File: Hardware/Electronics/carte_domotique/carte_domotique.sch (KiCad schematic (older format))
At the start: 21 parts, among them J1 Conn_02x06_Odd_Even, J10 Conn_01x04, J11 Conn_01x04, J12 Conn_01x04, J13 Conn_01x02, J14 Conn_01x02, J15 Conn_01x02, J16 Conn_01x02, J17 Conn_01x02, J18 Conn_01x02, J19 Conn_01x02, J2 Raspberry_Pi_2_3, J3 Conn_01x02, J4 Conn_01x05, J5 Conn_01x05, J6 Conn_01x03, J7 Conn_01x03, J8 Conn_01x03, J9 Conn_01x03

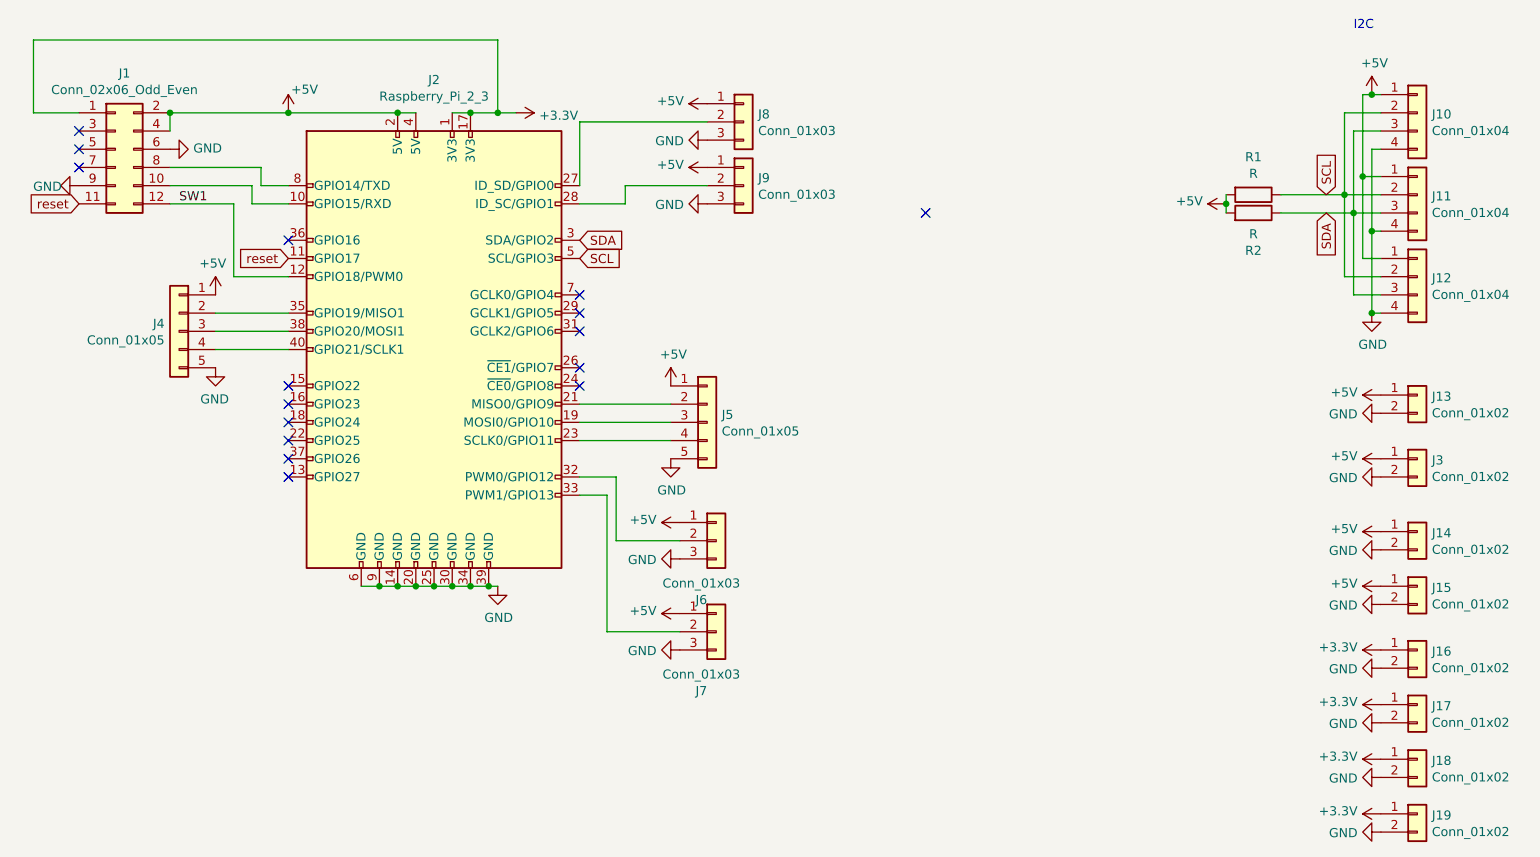
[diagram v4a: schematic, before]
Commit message: carte electronique
finalisation de la carte électronique
+ exportation 3D
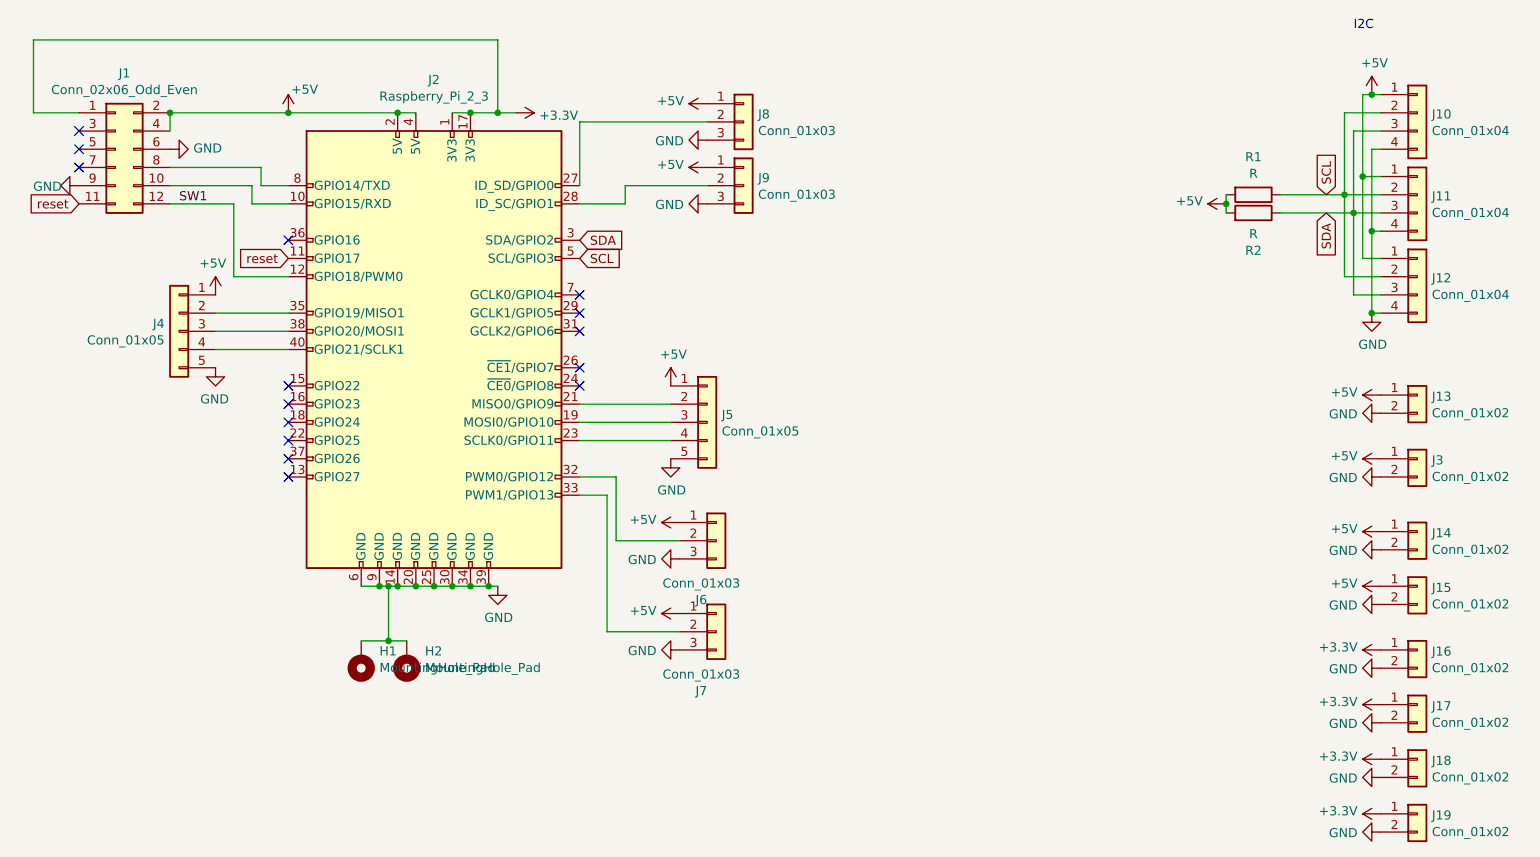
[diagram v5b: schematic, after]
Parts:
- added H1, H2: MountingHole_Pad, MountingHole:MountingHole_2.2mm_M2, symbol Mechanical:MountingHole_Pad
- J10, J11, J12: footprint Connector_PinHeader_2.54mm:PinHeader_1x04_P2.54mm_Vertical -> Connector_JST:JST_EH_B4B-EH-A_1x04_P2.50mm_Vertical
- J13, J14, J15, J16, J17, J18, J19, J3: footprint Connector_PinHeader_2.54mm:PinHeader_1x02_P2.54mm_Vertical -> Connector_JST:JST_EH_B2B-EH-A_1x02_P2.50mm_Vertical
- J4, J5: footprint Connector_PinHeader_2.54mm:PinHeader_1x05_P2.54mm_Vertical -> Connector_JST:JST_EH_B5B-EH-A_1x05_P2.50mm_Vertical
- J6, J7, J8, J9: footprint Connector_PinHeader_2.54mm:PinHeader_1x03_P2.54mm_Vertical -> Connector_JST:JST_EH_B3B-EH-A_1x03_P2.50mm_Vertical
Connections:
- net GND: now also H1.1, H2.1
- no-connect marks 16 -> 15
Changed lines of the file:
@@
 F 0 "J10" H 10230 1192 50  0000 L CNN
 F 1 "Conn_01x04" H 10230 1101 50  0000 L CNN
-F 2 "Connector_PinHeader_2.54mm:PinHeader_1x04_P2.54mm_Vertical" H 10150 1200 50  0001 C CNN
+F 2 "Connector_JST:JST_EH_B4B-EH-A_1x04_P2.50mm_Vertical" H 10150 1200 50  0001 C CNN
 F 3 "~" H 10150 1200 50  0001 C CNN
 	1    10150 1200
@@
 F 0 "J11" H 10230 1642 50  0000 L CNN
 F 1 "Conn_01x04" H 10230 1551 50  0000 L CNN
-F 2 "Connector_PinHeader_2.54mm:PinHeader_1x04_P2.54mm_Vertical" H 10150 1650 50  0001 C CNN
+F 2 "Connector_JST:JST_EH_B4B-EH-A_1x04_P2.50mm_Vertical" H 10150 1650 50  0001 C CNN
 F 3 "~" H 10150 1650 50  0001 C CNN
 	1    10150 1650
@@
 F 0 "J12" H 10230 2092 50  0000 L CNN
 F 1 "Conn_01x04" H 10230 2001 50  0000 L CNN
-F 2 "Connector_PinHeader_2.54mm:PinHeader_1x04_P2.54mm_Vertical" H 10150 2100 50  0001 C CNN
+F 2 "Connector_JST:JST_EH_B4B-EH-A_1x04_P2.50mm_Vertical" H 10150 2100 50  0001 C CNN
 F 3 "~" H 10150 2100 50  0001 C CNN
 	1    10150 2100
@@
 F 0 "J5" H 6330 2942 50  0000 L CNN
 F 1 "Conn_01x05" H 6330 2851 50  0000 L CNN
-F 2 "Connector_PinHeader_2.54mm:PinHeader_1x05_P2.54mm_Vertical" H 6250 2900 50  0001 C CNN
+F 2 "Connector_JST:JST_EH_B5B-EH-A_1x05_P2.50mm_Vertical" H 6250 2900 50  0001 C CNN
 F 3 "~" H 6250 2900 50  0001 C CNN
 	1    6250 2900
@@
 F 0 "J4" H 3430 2442 50  0000 L CNN
 F 1 "Conn_01x05" H 3430 2351 50  0000 L CNN
-F 2 "Connector_PinHeader_2.54mm:PinHeader_1x05_P2.54mm_Vertical" H 3350 2400 50  0001 C CNN
+F 2 "Connector_JST:JST_EH_B5B-EH-A_1x05_P2.50mm_Vertical" H 3350 2400 50  0001 C CNN
 F 3 "~" H 3350 2400 50  0001 C CNN
 	1    3350 2400
@@
 F 0 "J13" H 10230 2742 50  0000 L CNN
 F 1 "Conn_01x02" H 10230 2651 50  0000 L CNN
-F 2 "Connector_PinHeader_2.54mm:PinHeader_1x02_P2.54mm_Vertical" H 10150 2750 50  0001 C CNN
+F 2 "Connector_JST:JST_EH_B2B-EH-A_1x02_P2.50mm_Vertical" H 10150 2750 50  0001 C CNN
 F 3 "~" H 10150 2750 50  0001 C CNN
 	1    10150 2750
@@
 F 0 "J3" H 10230 3092 50  0000 L CNN
 F 1 "Conn_01x02" H 10230 3001 50  0000 L CNN
-F 2 "Connector_PinHeader_2.54mm:PinHeader_1x02_P2.54mm_Vertical" H 10150 3100 50  0001 C CNN
+F 2 "Connector_JST:JST_EH_B2B-EH-A_1x02_P2.50mm_Vertical" H 10150 3100 50  0001 C CNN
 F 3 "~" H 10150 3100 50  0001 C CNN
 	1    10150 3100
@@
 F 0 "J14" H 10230 3492 50  0000 L CNN
 F 1 "Conn_01x02" H 10230 3401 50  0000 L CNN
-F 2 "Connector_PinHeader_2.54mm:PinHeader_1x02_P2.54mm_Vertical" H 10150 3500 50  0001 C CNN
+F 2 "Connector_JST:JST_EH_B2B-EH-A_1x02_P2.50mm_Vertical" H 10150 3500 50  0001 C CNN
 F 3 "~" H 10150 3500 50  0001 C CNN
 	1    10150 3500
@@
 F 0 "J15" H 10230 3792 50  0000 L CNN
 F 1 "Conn_01x02" H 10230 3701 50  0000 L CNN
-F 2 "Connector_PinHeader_2.54mm:PinHeader_1x02_P2.54mm_Vertical" H 10150 3800 50  0001 C CNN
+F 2 "Connector_JST:JST_EH_B2B-EH-A_1x02_P2.50mm_Vertical" H 10150 3800 50  0001 C CNN
 F 3 "~" H 10150 3800 50  0001 C CNN
 	1    10150 3800
@@
 	0    -1   -1   0
 $EndComp
-$Comp
-L Connector_Generic:Conn_01x03 J8
-U 1 1 618E2FDE
-P 6450 1250
-F 0 "J8" H 6530 1292 50  0000 L CNN
-F 1 "Conn_01x03" H 6530 1201 50  0000 L CNN
-F 2 "Connector_PinHeader_2.54mm:PinHeader_1x03_P2.54mm_Vertical" H 6450 1250 50  0001 C CNN
-F 3 "~" H 6450 1250 50  0001 C CNN
-	1    6450 1250
-	1    0    0    -1
-$EndComp
-$Comp
-L Connector_Generic:Conn_01x03 J9
-U 1 1 618E744A
-P 6450 1600
-F 0 "J9" H 6530 1642 50  0000 L CNN
-F 1 "Conn_01x03" H 6530 1551 50  0000 L CNN
-F 2 "Connector_PinHeader_2.54mm:PinHeader_1x03_P2.54mm_Vertical" H 6450 1600 50  0001 C CNN
-F 3 "~" H 6450 1600 50  0001 C CNN
-	1    6450 1600
-	1    0    0    -1
-$EndComp
 Wire Wire Line
 	5550 1600 5550 1250
 Wire Wire Line
-	5550 1250 6250 1250
-Wire Wire Line
 	5800 1700 5800 1600
-Wire Wire Line
-	5800 1600 6250 1600
-$Comp
-L power:+5V #PWR0120
-U 1 1 618F0EC0
-P 6250 1150
-F 0 "#PWR0120" H 6250 1000 50  0001 C CNN
-F 1 "+5V" V 6265 1278 50  0000 L CNN
-F 2 "" H 6250 1150 50  0001 C CNN
-F 3 "" H 6250 1150 50  0001 C CNN
-	1    6250 1150
-	0    -1   -1   0
-$EndComp
-$Comp
-L power:+5V #PWR0121
-U 1 1 618F2F30
-P 6250 1500
-F 0 "#PWR0121" H 6250 1350 50  0001 C CNN
-F 1 "+5V" V 6265 1628 50  0000 L CNN
-F 2 "" H 6250 1500 50  0001 C CNN
-F 3 "" H 6250 1500 50  0001 C CNN
-	1    6250 1500
-	0    -1   -1   0
-$EndComp
 $Comp
 L Connector_Generic:Conn_01x03 J6
@@
 F 0 "J6" H 6218 3225 50  0000 C CNN
 F 1 "Conn_01x03" H 6218 3316 50  0000 C CNN
-F 2 "Connector_PinHeader_2.54mm:PinHeader_1x03_P2.54mm_Vertical" H 6300 3550 50  0001 C CNN
+F 2 "Connector_JST:JST_EH_B3B-EH-A_1x03_P2.50mm_Vertical" H 6300 3550 50  0001 C CNN
 F 3 "~" H 6300 3550 50  0001 C CNN
 	1    6300 3550
@@
 F 0 "J7" H 6218 3725 50  0000 C CNN
 F 1 "Conn_01x03" H 6218 3816 50  0000 C CNN
-F 2 "Connector_PinHeader_2.54mm:PinHeader_1x03_P2.54mm_Vertical" H 6300 4050 50  0001 C CNN
+F 2 "Connector_JST:JST_EH_B3B-EH-A_1x03_P2.50mm_Vertical" H 6300 4050 50  0001 C CNN
 F 3 "~" H 6300 4050 50  0001 C CNN
 	1    6300 4050
@@
 $EndComp
 $Comp
-L power:GND #PWR0124
-U 1 1 618FB650
-P 6250 1350
-F 0 "#PWR0124" H 6250 1100 50  0001 C CNN
-F 1 "GND" V 6255 1222 50  0000 R CNN
-F 2 "" H 6250 1350 50  0001 C CNN
-F 3 "" H 6250 1350 50  0001 C CNN
-	1    6250 1350
-	0    1    1    0
-$EndComp
-$Comp
-L power:GND #PWR0125
-U 1 1 618FBE1C
-P 6250 1700
-F 0 "#PWR0125" H 6250 1450 50  0001 C CNN
-F 1 "GND" V 6255 1572 50  0000 R CNN
-F 2 "" H 6250 1700 50  0001 C CNN
-F 3 "" H 6250 1700 50  0001 C CNN
-	1    6250 1700
-	0    1    1    0
-$EndComp
-$Comp
 L power:GND #PWR0126
 U 1 1 618FBFFE
@@
 F 0 "J16" H 10230 4142 50  0000 L CNN
 F 1 "Conn_01x02" H 10230 4051 50  0000 L CNN
-F 2 "Connector_PinHeader_2.54mm:PinHeader_1x02_P2.54mm_Vertical" H 10150 4150 50  0001 C CNN
+F 2 "Connector_JST:JST_EH_B2B-EH-A_1x02_P2.50mm_Vertical" H 10150 4150 50  0001 C CNN
 F 3 "~" H 10150 4150 50  0001 C CNN
 	1    10150 4150
@@
 F 0 "J17" H 10230 4442 50  0000 L CNN
 F 1 "Conn_01x02" H 10230 4351 50  0000 L CNN
-F 2 "Connector_PinHeader_2.54mm:PinHeader_1x02_P2.54mm_Vertical" H 10150 4450 50  0001 C CNN
+F 2 "Connector_JST:JST_EH_B2B-EH-A_1x02_P2.50mm_Vertical" H 10150 4450 50  0001 C CNN
 F 3 "~" H 10150 4450 50  0001 C CNN
 	1    10150 4450
@@
 F 0 "J18" H 10230 4742 50  0000 L CNN
 F 1 "Conn_01x02" H 10230 4651 50  0000 L CNN
-F 2 "Connector_PinHeader_2.54mm:PinHeader_1x02_P2.54mm_Vertical" H 10150 4750 50  0001 C CNN
+F 2 "Connector_JST:JST_EH_B2B-EH-A_1x02_P2.50mm_Vertical" H 10150 4750 50  0001 C CNN
 F 3 "~" H 10150 4750 50  0001 C CNN
 	1    10150 4750
@@
 F 0 "J19" H 10230 5042 50  0000 L CNN
 F 1 "Conn_01x02" H 10230 4951 50  0000 L CNN
-F 2 "Connector_PinHeader_2.54mm:PinHeader_1x02_P2.54mm_Vertical" H 10150 5050 50  0001 C CNN
+F 2 "Connector_JST:JST_EH_B2B-EH-A_1x02_P2.50mm_Vertical" H 10150 5050 50  0001 C CNN
 F 3 "~" H 10150 5050 50  0001 C CNN
 	1    10150 5050
@@
 NoConn ~ 3950 3100
 NoConn ~ 3950 3200
-NoConn ~ 7450 1750
 Connection ~ 4550 1200
 Wire Wire Line
@@
 	4550 1200 4650 1200
 Wire Wire Line
-	4550 3800 4450 3800
+	4550 3800 4500 3800
 Wire Wire Line
 	4450 3800 4350 3800
@@
 reset
 $Comp
-L power:+5V #PWR?
+L power:+5V #PWR0136
 U 1 1 61C061AB
 P 3950 1200
-F 0 "#PWR?" H 3950 1050 50  0001 C CNN
+F 0 "#PWR0136" H 3950 1050 50  0001 C CNN
 F 1 "+5V" H 3965 1328 50  0000 L CNN
 F 2 "" H 3950 1200 50  0001 C CNN
@@
 Wire Wire Line
 	3950 1200 4550 1200
+$Comp
+L Mechanical:MountingHole_Pad H2
+U 1 1 61D359AA
+P 4600 4200
+F 0 "H2" H 4500 4157 50  0000 R CNN
+F 1 "MountingHole_Pad" H 4500 4248 50  0000 R CNN
+F 2 "MountingHole:MountingHole_2.2mm_M2" H 4600 4200 50  0001 C CNN
+F 3 "~" H 4600 4200 50  0001 C CNN
+	1    4600 4200
+	-1   0    0    1
+$EndComp
+$Comp
+L Mechanical:MountingHole_Pad H1
+U 1 1 61D37EF2
+P 4350 4200
+F 0 "H1" H 4250 4157 50  0000 R CNN
+F 1 "MountingHole_Pad" H 4250 4248 50  0000 R CNN
+F 2 "MountingHole:MountingHole_2.2mm_M2" H 4350 4200 50  0001 C CNN
+F 3 "~" H 4350 4200 50  0001 C CNN
+	1    4350 4200
+	-1   0    0    1
+$EndComp
+Wire Wire Line
+	4350 4100 4500 4100
+Wire Wire Line
+	4500 4100 4500 3800
+Connection ~ 4500 4100
+Wire Wire Line
+	4500 4100 4600 4100
+Connection ~ 4500 3800
+Wire Wire Line
+	4500 3800 4450 3800
+$Comp
+L power:GND #PWR0125
+U 1 1 618FBE1C
+P 6250 1700
+F 0 "#PWR0125" H 6250 1450 50  0001 C CNN
+F 1 "GND" V 6255 1572 50  0000 R CNN
+F 2 "" H 6250 1700 50  0001 C CNN
+F 3 "" H 6250 1700 50  0001 C CNN
+	1    6250 1700
+	0    1    1    0
+$EndComp
+$Comp
+L power:GND #PWR0124
+U 1 1 618FB650
+P 6250 1350
+F 0 "#PWR0124" H 6250 1100 50  0001 C CNN
+F 1 "GND" V 6255 1222 50  0000 R CNN
+F 2 "" H 6250 1350 50  0001 C CNN
+F 3 "" H 6250 1350 50  0001 C CNN
+	1    6250 1350
+	0    1    1    0
+$EndComp
+$Comp
+L power:+5V #PWR0121
+U 1 1 618F2F30
+P 6250 1500
+F 0 "#PWR0121" H 6250 1350 50  0001 C CNN
+F 1 "+5V" V 6265 1628 50  0000 L CNN
+F 2 "" H 6250 1500 50  0001 C CNN
+F 3 "" H 6250 1500 50  0001 C CNN
+	1    6250 1500
+	0    -1   -1   0
+$EndComp
+$Comp
+L power:+5V #PWR0120
+U 1 1 618F0EC0
+P 6250 1150
+F 0 "#PWR0120" H 6250 1000 50  0001 C CNN
+F 1 "+5V" V 6265 1278 50  0000 L CNN
+F 2 "" H 6250 1150 50  0001 C CNN
+F 3 "" H 6250 1150 50  0001 C CNN
+	1    6250 1150
+	0    -1   -1   0
+$EndComp
+Wire Wire Line
+	5800 1600 6250 1600
+Wire Wire Line
+	5550 1250 6250 1250
+$Comp
+L Connector_Generic:Conn_01x03 J9
+U 1 1 618E744A
+P 6450 1600
+F 0 "J9" H 6530 1642 50  0000 L CNN
+F 1 "Conn_01x03" H 6530 1551 50  0000 L CNN
+F 2 "Connector_JST:JST_EH_B3B-EH-A_1x03_P2.50mm_Vertical" H 6450 1600 50  0001 C CNN
+F 3 "~" H 6450 1600 50  0001 C CNN
+	1    6450 1600
+	1    0    0    -1
+$EndComp
+$Comp
+L Connector_Generic:Conn_01x03 J8
+U 1 1 618E2FDE
+P 6450 1250
+F 0 "J8" H 6530 1292 50  0000 L CNN
+F 1 "Conn_01x03" H 6530 1201 50  0000 L CNN
+F 2 "Connector_JST:JST_EH_B3B-EH-A_1x03_P2.50mm_Vertical" H 6450 1250 50  0001 C CNN
+F 3 "~" H 6450 1250 50  0001 C CNN
+	1    6450 1250
+	1    0    0    -1
+$EndComp
 $EndSCHEMATC
